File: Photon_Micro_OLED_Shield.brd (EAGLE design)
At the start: 35.6 x 35.6 mm, 28 parts

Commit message: qc fixes
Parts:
- C1: device SparkFun-Passives:0805 -> SparkFun-Capacitors:0805-CAP
- C2, C3: value 1uF X5R -> 1uF; device SparkFun-Passives:0805 -> SparkFun-Capacitors:0805-CAP
- C5: value 4.7uF/16V -> 4.7uF; device SparkFun-Passives:1206 -> SparkFun-Capacitors:1206-CAP
- moved FRAME1 49.1 mm to (0.00, -12.7)
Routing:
- net MOSI: track 15.6 -> 16.4 mm
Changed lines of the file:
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@@
 <layer number="45" name="Holes" color="7" fill="1" visible="yes" active="yes"/>
 <layer number="46" name="Milling" color="3" fill="1" visible="no" active="yes"/>
-<layer number="47" name="Measures" color="7" fill="1" visible="yes" active="yes"/>
-<layer number="48" name="Document" color="7" fill="1" visible="yes" active="yes"/>
+<layer number="47" name="Measures" color="7" fill="1" visible="no" active="yes"/>
+<layer number="48" name="Document" color="7" fill="1" visible="no" active="yes"/>
 <layer number="49" name="Reference" color="7" fill="1" visible="no" active="yes"/>
 <layer number="50" name="dxf" color="7" fill="1" visible="no" active="no"/>
@@
 <text x="23.876" y="17.78" size="0.889" layer="21" font="vector" ratio="15" rot="R270" align="center">0</text>
 <text x="25.908" y="17.78" size="0.889" layer="21" font="vector" ratio="15" rot="R270" align="center">1</text>
-<text x="19.05" y="-60.96" size="1.778" layer="51" ratio="15">Ben Leduc-Mills</text>
+<text x="26.67" y="-12.7" size="1.778" layer="51" ratio="15">Ben Leduc-Mills</text>
 <text x="12.573" y="0.127" size="1.016" layer="16" font="vector" ratio="23" rot="MR180">v01</text>
 <text x="25.4" y="24.765" size="0.889" layer="21" font="vector" ratio="15" rot="R270" align="center-right">D1</text>
@@
 </autorouter>
 <elements>
-<element name="OLED1" library="microView-temp" package="OLED-0.66-64X48" value="OLED0.66" x="19.304" y="12.065" rot="MR90"/>
-<element name="FRAME1" library="SparkFun-Aesthetics" package="CREATIVE_COMMONS" value="" x="-8.89" y="-60.96">
-<attribute name="VERSION" value="v01" x="-8.89" y="-60.96" size="1.778" layer="27" display="off"/>
-<attribute name="DESIGNER" value="NAME" x="-8.89" y="-60.96" size="1.778" layer="27" display="off"/>
-</element>
-<element name="C1" library="SparkFun-Passives" package="0805" value="2.2uF" x="19.812" y="29.845" rot="R180"/>
-<element name="C2" library="SparkFun-Passives" package="0805" value="1uF X5R" x="19.812" y="14.605"/>
-<element name="C3" library="SparkFun-Passives" package="0805" value="1uF X5R" x="19.812" y="12.065"/>
-<element name="C4" library="SparkFun-Passives" package="0603-CAP" value="1uF" x="19.812" y="19.685"/>
-<element name="C5" library="SparkFun-Passives" package="1206" value="4.7uF/16V" x="19.812" y="27.305" rot="R180"/>
-<element name="R1" library="SparkFun-Passives" package="0603-RES" value="390k" x="19.812" y="24.765"/>
+<element name="OLED1" library="microView-temp" package="OLED-0.66-64X48" value="OLED0.66" x="19.304" y="12.065" rot="MR90">
+<attribute name="PROD_ID" value="LCD-12019" x="19.304" y="12.065" size="1.778" layer="28" rot="MR90" display="off"/>
+</element>
+<element name="FRAME1" library="SparkFun-Aesthetics" package="CREATIVE_COMMONS" value="" x="0" y="-12.7">
+<attribute name="VERSION" value="v01" x="0" y="-12.7" size="1.778" layer="27" display="off"/>
+<attribute name="DESIGNER" value="NAME" x="0" y="-12.7" size="1.778" layer="27" display="off"/>
+</element>
+<element name="C1" library="SparkFun-Capacitors" package="0805-CAP" value="2.2uF" x="19.812" y="29.845" rot="R180">
+<attribute name="PROD_ID" value="CAP-11624" x="19.812" y="29.845" size="1.778" layer="27" rot="R180" display="off"/>
+<attribute name="VALUE" value="2.2uF" x="19.812" y="29.845" size="1.778" layer="27" rot="R180" display="off"/>
+</element>
+<element name="C2" library="SparkFun-Capacitors" package="0805-CAP" value="1uF" x="19.812" y="14.605"/>
+<element name="C3" library="SparkFun-Capacitors" package="0805-CAP" value="1uF" x="19.812" y="12.065"/>
+<element name="C4" library="SparkFun-Passives" package="0603-CAP" value="1uF" x="19.812" y="19.685">
+<attribute name="PROD_ID" value="CAP-00868" x="19.812" y="19.685" size="1.778" layer="27" display="off"/>
+</element>
+<element name="C5" library="SparkFun-Capacitors" package="1206-CAP" value="4.7uF" x="19.812" y="27.305" rot="R180">
+<attribute name="PROD_ID" value="CAP-10300" x="19.812" y="27.305" size="1.778" layer="27" rot="R180" display="off"/>
+<attribute name="VALUE" value="4.7uF" x="19.812" y="27.305" size="1.778" layer="27" rot="R180" display="off"/>
+</element>
+<element name="R1" library="SparkFun-Passives" package="0603-RES" value="390k" x="19.812" y="24.765">
+<attribute name="PROD_ID" value="RES-12024" x="19.812" y="24.765" size="1.778" layer="27" display="off"/>
+</element>
 <element name="SJ3" library="SparkFun-Passives" package="PAD-JUMPER-2-NC_BY_TRACE_YES_SILK" value="" x="16.637" y="18.415" rot="R90"/>
-<element name="R2" library="SparkFun-Passives" package="0603-RES" value="10k" x="19.812" y="22.225" rot="R180"/>
+<element name="R2" library="SparkFun-Passives" package="0603-RES" value="10k" x="19.812" y="22.225" rot="R180">
+<attribute name="PROD_ID" value="RES-00824" x="19.812" y="22.225" size="1.778" layer="27" rot="R180" display="off"/>
+</element>
 <element name="FID1" library="SparkFun-Aesthetics" package="FIDUCIAL-1X2" value="FIDUCIAL1X2" x="5.08" y="3.81" rot="R270"/>
 <element name="FID2" library="SparkFun-Aesthetics" package="FIDUCIAL-1X2" value="FIDUCIAL1X2" x="38.1" y="29.21" rot="R270"/>
 <element name="SJ5" library="SparkFun-Passives" package="PAD-JUMPER-2-NO_YES_SILK" value="" x="24.892" y="23.495" rot="R180"/>
 <element name="TP1" library="SparkFun-Passives" package="PAD.03X.05" value="TEST-POINT3X5" x="23.622" y="28.575" rot="R270"/>
-<element name="C6" library="SparkFun-Passives" package="0603-CAP" value="1uF" x="19.812" y="17.145"/>
+<element name="C6" library="SparkFun-Passives" package="0603-CAP" value="1uF" x="19.812" y="17.145">
+<attribute name="PROD_ID" value="CAP-00868" x="19.812" y="17.145" size="1.778" layer="27" display="off"/>
+</element>
 <element name="SJ1" library="SparkFun-Passives" package="PAD-JUMPER-3-2OF3_NC_BY_PASTE_YES_SILK_FULL_BOX" value="BS1" x="24.892" y="11.684" rot="R180"/>
 <element name="SJ2" library="SparkFun-Passives" package="PAD-JUMPER-3-2OF3_NC_BY_PASTE_YES_SILK_FULL_BOX" value="BS2" x="24.892" y="15.875" rot="R180"/>
@@
 <contactref element="OLED1" pad="16"/>
 <contactref element="SJ10" pad="2"/>
-<wire x1="23.4315" y1="3.81" x2="24.765" y2="5.1435" width="0.2032" layer="1"/>
-<wire x1="11.557" y1="3.81" x2="23.4315" y2="3.81" width="0.2032" layer="1"/>
 <wire x1="11.43" y1="3.937" x2="11.557" y2="3.81" width="0.1778" layer="1"/>
 <wire x1="11.43" y1="3.81" x2="11.43" y2="3.937" width="0.1778" layer="1"/>
@@
 <wire x1="17.907" y1="21.844" x2="19.275" y2="21.844" width="0.2032" layer="16"/>
 <wire x1="19.275" y1="21.844" x2="19.304" y2="21.815" width="0.2032" layer="16"/>
-<wire x1="24.892" y1="5.969" x2="24.765" y2="5.842" width="0.2032" layer="1"/>
-<wire x1="24.765" y1="5.842" x2="24.765" y2="5.1435" width="0.2032" layer="1"/>
 <wire x1="15.113" y1="19.05" x2="11.811" y2="19.05" width="0.2032" layer="16"/>
 <wire x1="11.811" y1="19.05" x2="11.43" y2="18.669" width="0.2032" layer="16"/>
+<wire x1="11.557" y1="3.81" x2="24.003" y2="3.81" width="0.2032" layer="1"/>
+<wire x1="24.003" y1="3.81" x2="24.765" y2="4.572" width="0.2032" layer="1"/>
+<wire x1="24.765" y1="4.572" x2="24.765" y2="5.842" width="0.2032" layer="1"/>
+<wire x1="24.765" y1="5.842" x2="24.892" y2="5.969" width="0.2032" layer="1"/>
 </signal>
 <signal name="RESET">
@@
 <contactref element="SJ8" pad="3"/>
 <wire x1="24.0792" y1="8.763" x2="23.9522" y2="8.89" width="0.2032" layer="1"/>
-<wire x1="23.9522" y1="8.89" x2="23.241" y2="8.89" width="0.2032" layer="1"/>
-<wire x1="23.241" y1="8.89" x2="21.971" y2="10.16" width="0.2032" layer="1"/>
-<wire x1="21.971" y1="10.16" x2="15.113" y2="10.16" width="0.2032" layer="1"/>
+<wire x1="23.749" y1="10.16" x2="15.113" y2="10.16" width="0.2032" layer="1"/>
 <wire x1="15.113" y1="10.16" x2="13.97" y2="11.303" width="0.2032" layer="1"/>
 <wire x1="13.97" y1="11.303" x2="13.97" y2="13.97" width="0.2032" layer="1"/>
 <wire x1="13.97" y1="13.97" x2="12.7" y2="15.24" width="0.2032" layer="1"/>
+<wire x1="23.749" y1="10.16" x2="24.003" y2="9.906" width="0.2032" layer="1"/>
+<wire x1="24.003" y1="9.906" x2="24.003" y2="8.8392" width="0.2032" layer="1"/>
+<wire x1="24.003" y1="8.8392" x2="24.0792" y2="8.763" width="0.2032" layer="1"/>
 </signal>
 <signal name="MISO">
@@
 <contactref element="JP3" pad="A3"/>
 <contactref element="SJ10" pad="3"/>
-<wire x1="24.0792" y1="5.969" x2="23.368" y2="5.969" width="0.2032" layer="1"/>
-<wire x1="23.368" y1="5.969" x2="21.844" y2="4.445" width="0.2032" layer="1"/>
-<wire x1="21.844" y1="4.445" x2="15.494" y2="4.445" width="0.2032" layer="1"/>
+<wire x1="23.368" y1="4.445" x2="15.494" y2="4.445" width="0.2032" layer="1"/>
 <wire x1="15.494" y1="4.445" x2="14.097" y2="5.842" width="0.2032" layer="1"/>
 <wire x1="14.097" y1="5.842" x2="14.097" y2="8.763" width="0.2032" layer="1"/>
 <wire x1="14.097" y1="8.763" x2="12.7" y2="10.16" width="0.2032" layer="1"/>
+<wire x1="23.368" y1="4.445" x2="24.003" y2="5.08" width="0.2032" layer="1"/>
+<wire x1="24.003" y1="5.08" x2="24.003" y2="5.8928" width="0.2032" layer="1"/>
+<wire x1="24.003" y1="5.8928" x2="24.0792" y2="5.969" width="0.2032" layer="1"/>
 </signal>
 <signal name="SS">

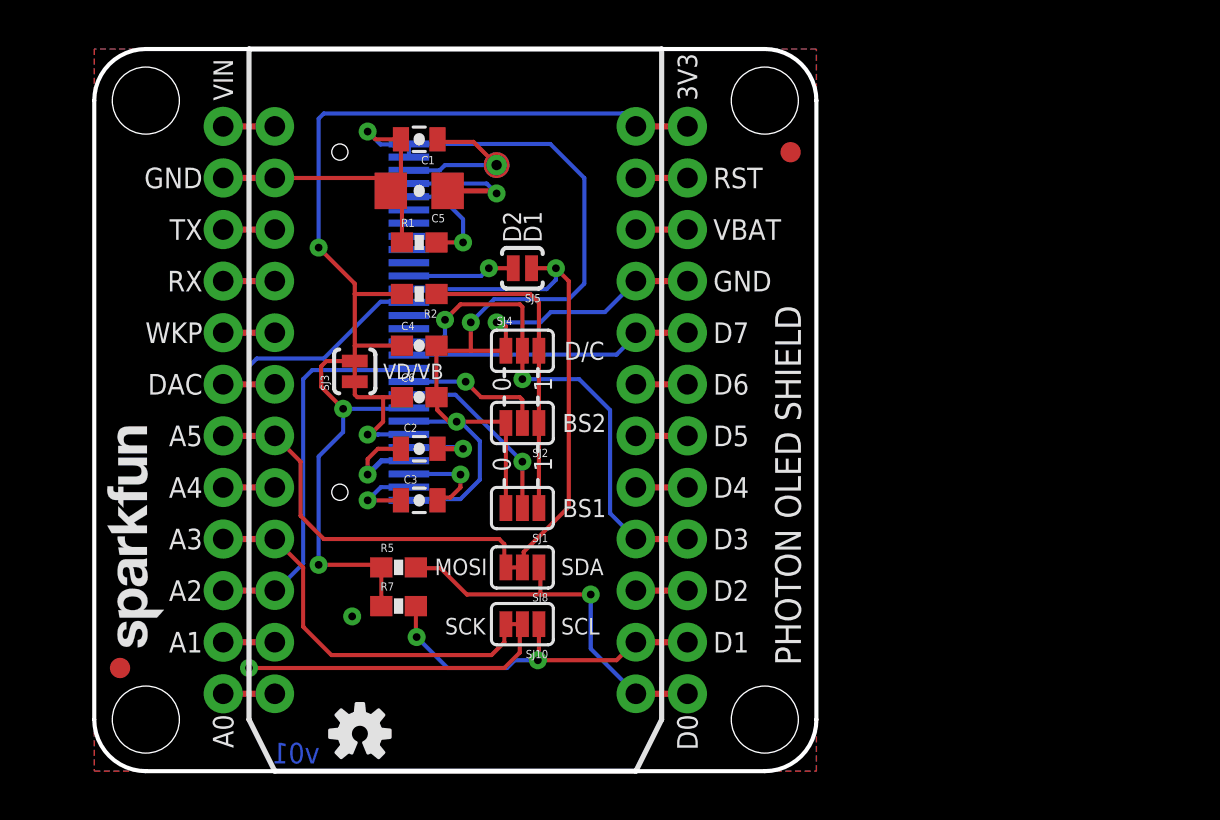
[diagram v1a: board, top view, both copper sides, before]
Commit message: new design
moved screen to top and extended board so it will work better with the
rest of the photon shields
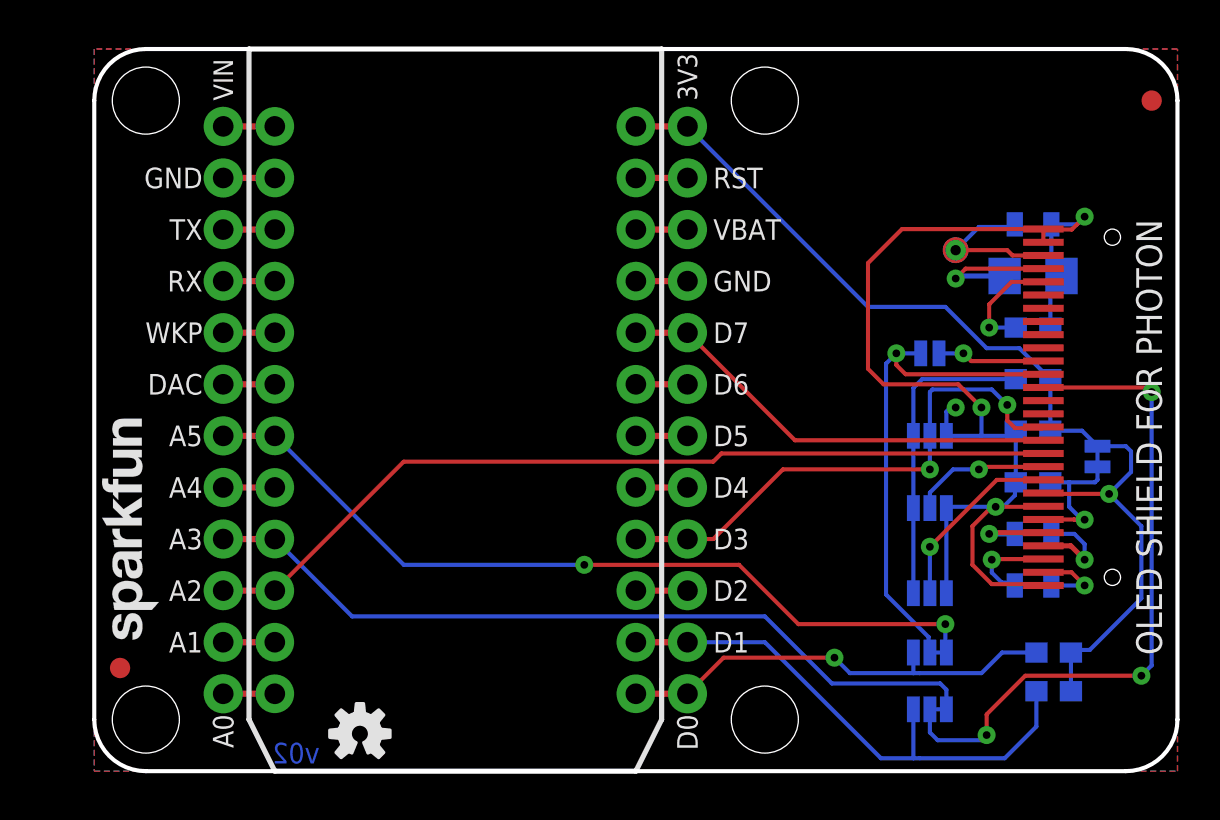
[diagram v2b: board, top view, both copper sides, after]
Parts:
- moved SJ3 36.8 mm to (53.2, 14.2), flipped to the bottom
- moved R5 32.5 mm to (51.1, 4.57), flipped to the bottom
- moved R7 32.5 mm to (51.1, 2.67), flipped to the bottom
- moved OLED1 31.5 mm to (50.5, 7.87), flipped to the top
- moved C1 30.5 mm to (50.0, 25.7), flipped to the bottom
- moved C2 30.5 mm to (50.0, 10.4), flipped to the bottom
- moved C3 30.5 mm to (50.0, 7.87), flipped to the bottom
- moved C4 30.5 mm to (50.0, 15.5), flipped to the bottom
- moved C5 30.5 mm to (50.0, 23.1), flipped to the bottom
- moved C6 30.5 mm to (50.0, 13.0), flipped to the bottom
- moved R1 30.5 mm to (50.0, 20.6), flipped to the bottom
- moved R2 30.5 mm to (50.0, 18.0), flipped to the bottom
- moved TP1 23.0 mm to (46.2, 24.4), flipped to the bottom
- moved TP2 23.0 mm to (46.2, 24.4), flipped to the top
- moved SJ1 20.5 mm to (45.0, 7.49), flipped to the bottom
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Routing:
- net SS: track 16.5 -> 40.6 mm
- net MOSI: track 16.4 -> 38.5 mm, vias 0 -> 2
- net SCK: track 16.6 -> 37.1 mm
- net GND: track 72.3 -> 59.5 mm, vias 5 -> 4
- net D1/SCL: track 15.4 -> 24.4 mm, vias 2 -> 0
- net D7: track 11.7 -> 19.7 mm
- net D0/SCK: track 39.3 -> 33.2 mm, vias 1 -> 3
- net VDD: track 54.1 -> 48.0 mm, vias 3 -> 1
- net D0/SDA: track 16.3 -> 19.7 mm
- net D/C: track 22.3 -> 24.1 mm
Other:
- board size 35.6 x 35.6 mm -> 53.3 x 35.6 mm
- board text added: "OLED SHIELD FOR PHOTON"
- board text added: "v02"
- board text removed: "PHOTON OLED SHIELD"
- board text removed: "v01"

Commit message: Adding gap between Photon and pin-break outs. Moving D/C to pin D6.
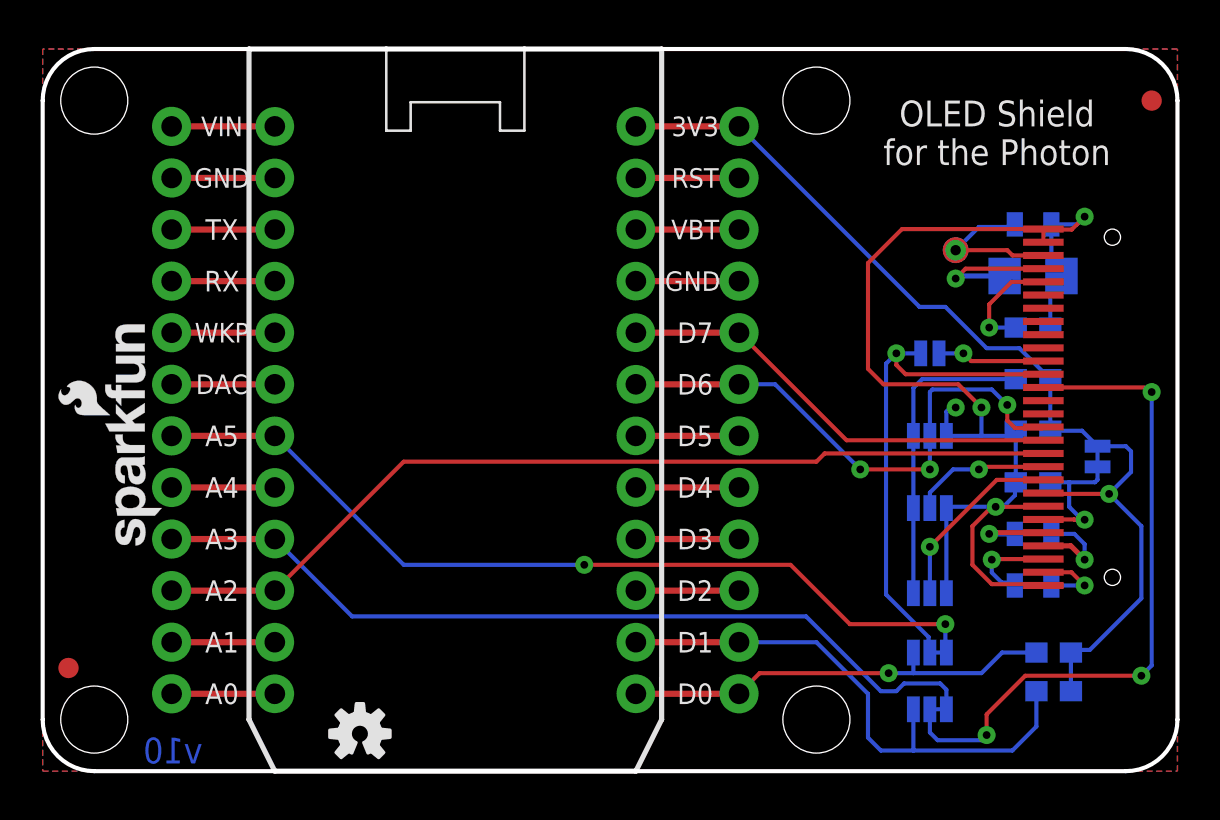
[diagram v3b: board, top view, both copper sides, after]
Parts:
- JP3: value SPARK_PHOTONTEMPLATE -> SPARK_PHOTONTEMPLATE_WIDE; device template_temp:SPARK_PHOTON_TEMPLATE -> template_temp:SPARK_PHOTON_TEMPLATE_WIDE
- LOGO1, LOGO2: value SFE_LOGO_NAME.1_INCH -> SFE_LOGO_NAME_FLAME.1_INCH; device SparkFun-Aesthetics:SFE_LOGO_NAME_.1 -> SparkFun-Aesthetics:SFE_LOGO_NAME_FLAME_.1
- moved LOGO2 16.9 mm to (7.11, 21.2), turned to 270 degrees
- moved LOGO1 4.71 mm to (7.24, 9.40)
- moved FID1 2.54 mm to (2.54, 3.81)
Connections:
- removed net D/C: JP3.16, JP3.D3, OLED1.13, SJ4.2
- new net D3: JP3.16, JP3.D3
- net D6: now also OLED1.13, SJ4.2
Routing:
- net D/C: track 24.1 -> 0.00 mm, vias 2 -> 0
- net D6: track 0.00 -> 21.8 mm, vias 0 -> 3
- net D0/SDA: track 19.7 -> 16.5 mm
- net VDD: track 48.0 -> 45.5 mm
- net D7: track 19.7 -> 17.2 mm
- net D1/SCL: track 24.4 -> 22.6 mm
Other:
- board size 53.3 x 35.6 mm -> 55.9 x 35.6 mm
- board text added: "OLED Shield for the Photon"
- board text added: "v10"
- board text removed: "OLED SHIELD FOR PHOTON"
- board text removed: "v02"
